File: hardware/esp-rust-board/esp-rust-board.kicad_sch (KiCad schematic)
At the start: 83 parts, among them J1 USB4105-GF-A, J2 MOTOR L, J3 MOTOR R, J4 BATT, J5 LED L, J6 LED R, Q1 DMG3415U, Q2 Si2319CDS, Q3 Si2319CDS, Q4 MMBT3904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

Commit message: Place components on PCB
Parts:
- removed J4: BATT, symbol Connector_Generic:Conn_01x02
- removed J5: LED L, Connector_JST:JST_PH_B2B-PH-SM4-TB_1x02-1MP_P2.00mm_Vertical, symbol Connector_Generic:Conn_01x02
- removed J6: LED R, Connector_JST:JST_PH_B2B-PH-SM4-TB_1x02-1MP_P2.00mm_Vertical, symbol Connector_Generic:Conn_01x02
- removed Q4, Q5: MMBT3904, Package_TO_SOT_SMD:SOT-23, symbol Transistor_BJT:MMBT3904
- removed R22, R24: 470R 1%, Resistor_SMD:R_0402_1005Metric, symbol Device:R_Small_US
- removed R23, R25: 10kR 1%, Resistor_SMD:R_0402_1005Metric, symbol Device:R_Small_US
- removed TP2: IMU_INT2, TestPoint:TestPoint_Pad_D1.0mm, symbol Connector:TestPoint
- added H1, H2: MountingHole_Pad, TestPoint:TestPoint_Keystone_5005-5009_Compact, symbol Mechanical:MountingHole_Pad
- added J7, J8: SERVO R, Connector_PinSocket_2.00mm:PinSocket_1x03_P2.00mm_Vertical, symbol Connector_Generic:Conn_01x03
- J2, J3: footprint Connector_JST:JST_PH_B2B-PH-SM4-TB_1x02-1MP_P2.00mm_Vertical -> Connector_PinHeader_2.00mm:PinHeader_1x02_P2.00mm_Vertical
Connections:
- net +BATT: now also H1.1, J7.2 (Pin_2), J8.2 (Pin_2)
- net GND: now also H2.1, J7.3 (Pin_3), J8.3 (Pin_3)
- net IO0: now also J7.1 (Pin_1)
- net IO20_RX: now also TP3.1; no longer TP1.1
- net IO21_TX: now also TP1.1; no longer TP3.1
- net IO4: now also R13.1
- net IO5: now also R20.1
- net IO6: now also J8.1 (Pin_1); no longer R20.1
- net IO7: now also R11.1; no longer R13.1
- net IO1: no longer names the net of U3.13 (GPIO1/ADC1_CH1/XTAL_32K_N)
- net IO2: no longer names the net of U3.5 (GPIO2/ADC1_CH2)
- net IO2: no longer R11.1
- net IO3: no longer names the net of U3.6 (GPIO3/ADC1_CH3)
- no-connect marks 18 -> 33
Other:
- note added: "Address: 0x0d (0001101b)"
- moved on the sheet: C12, C13, C17, C18, C20, C3, D11, J3, Q3, R12, R20, R21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

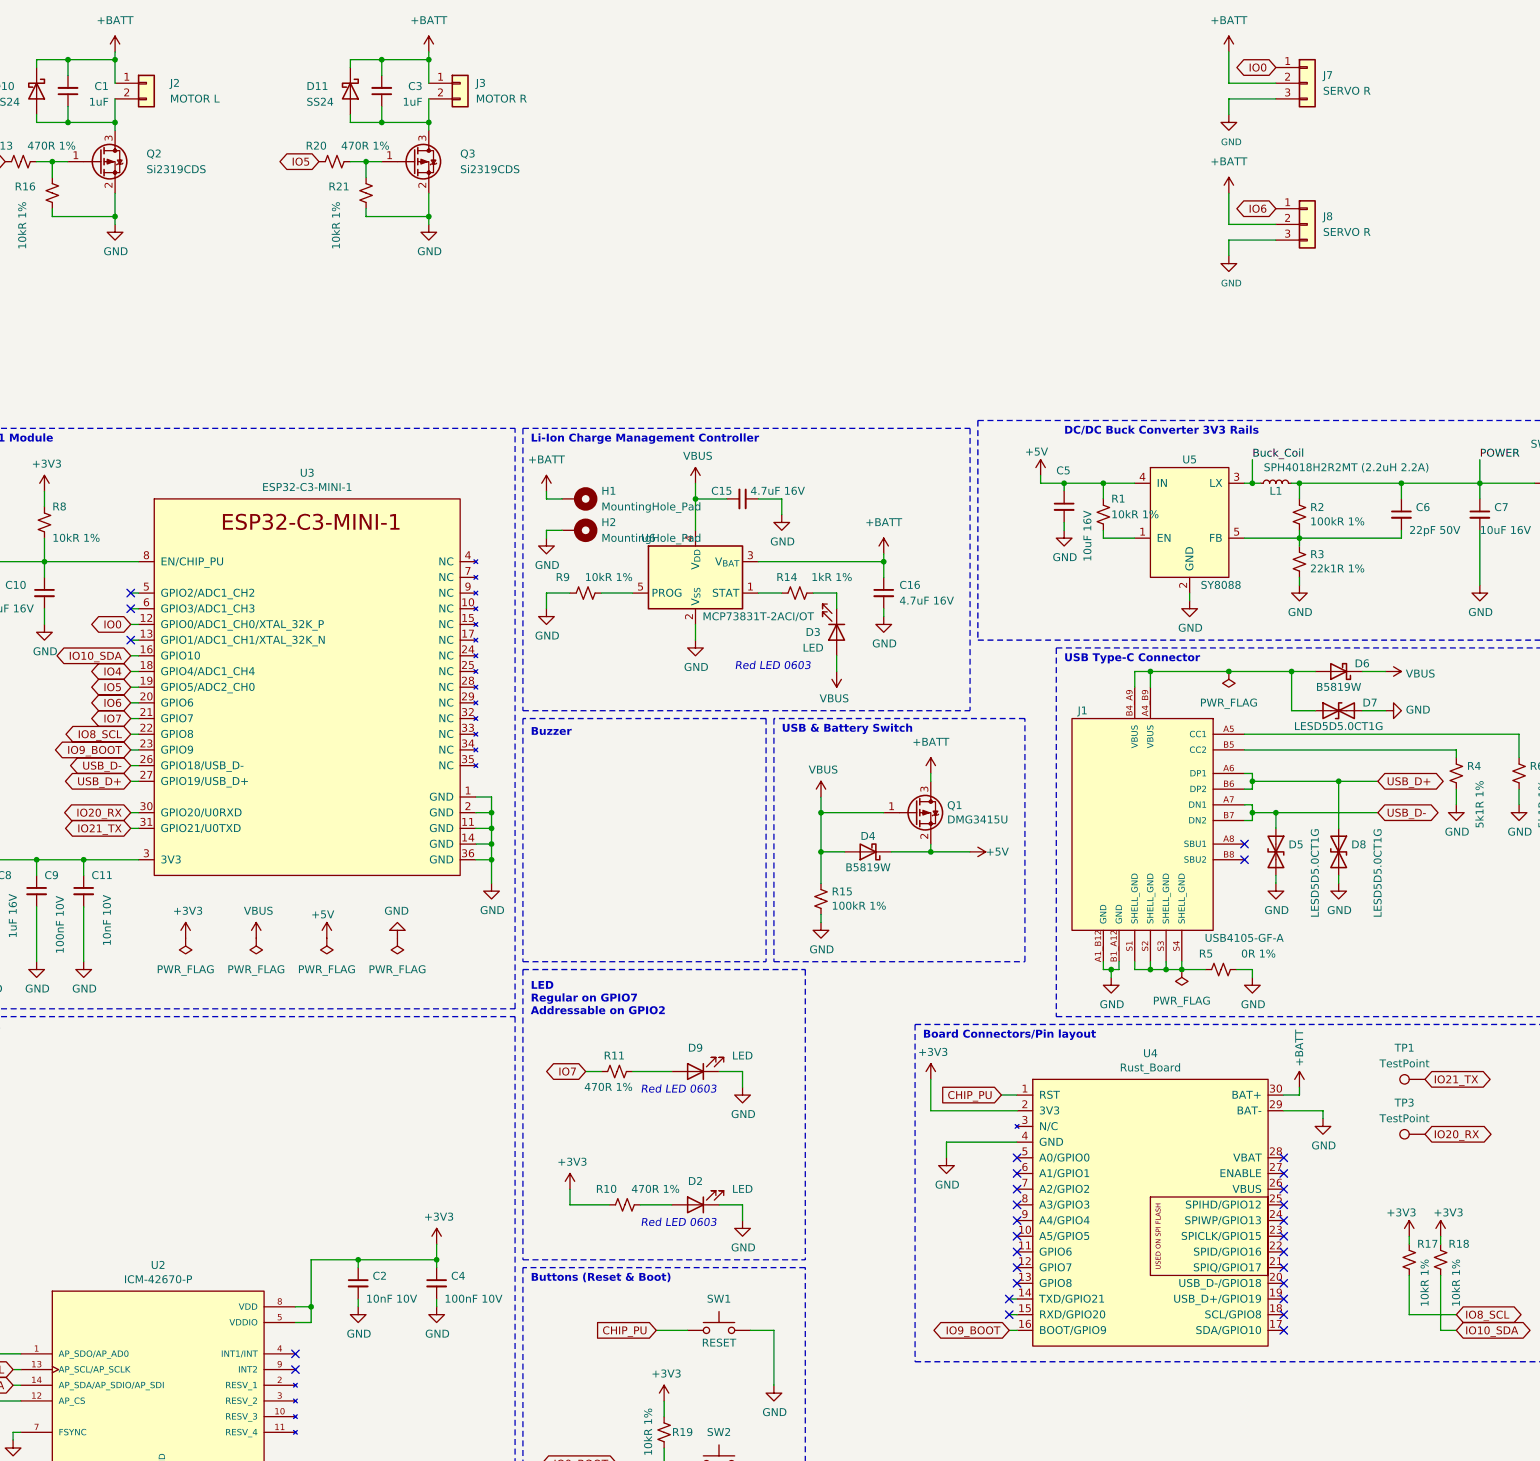
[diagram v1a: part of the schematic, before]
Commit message: Add missing LCSC parts
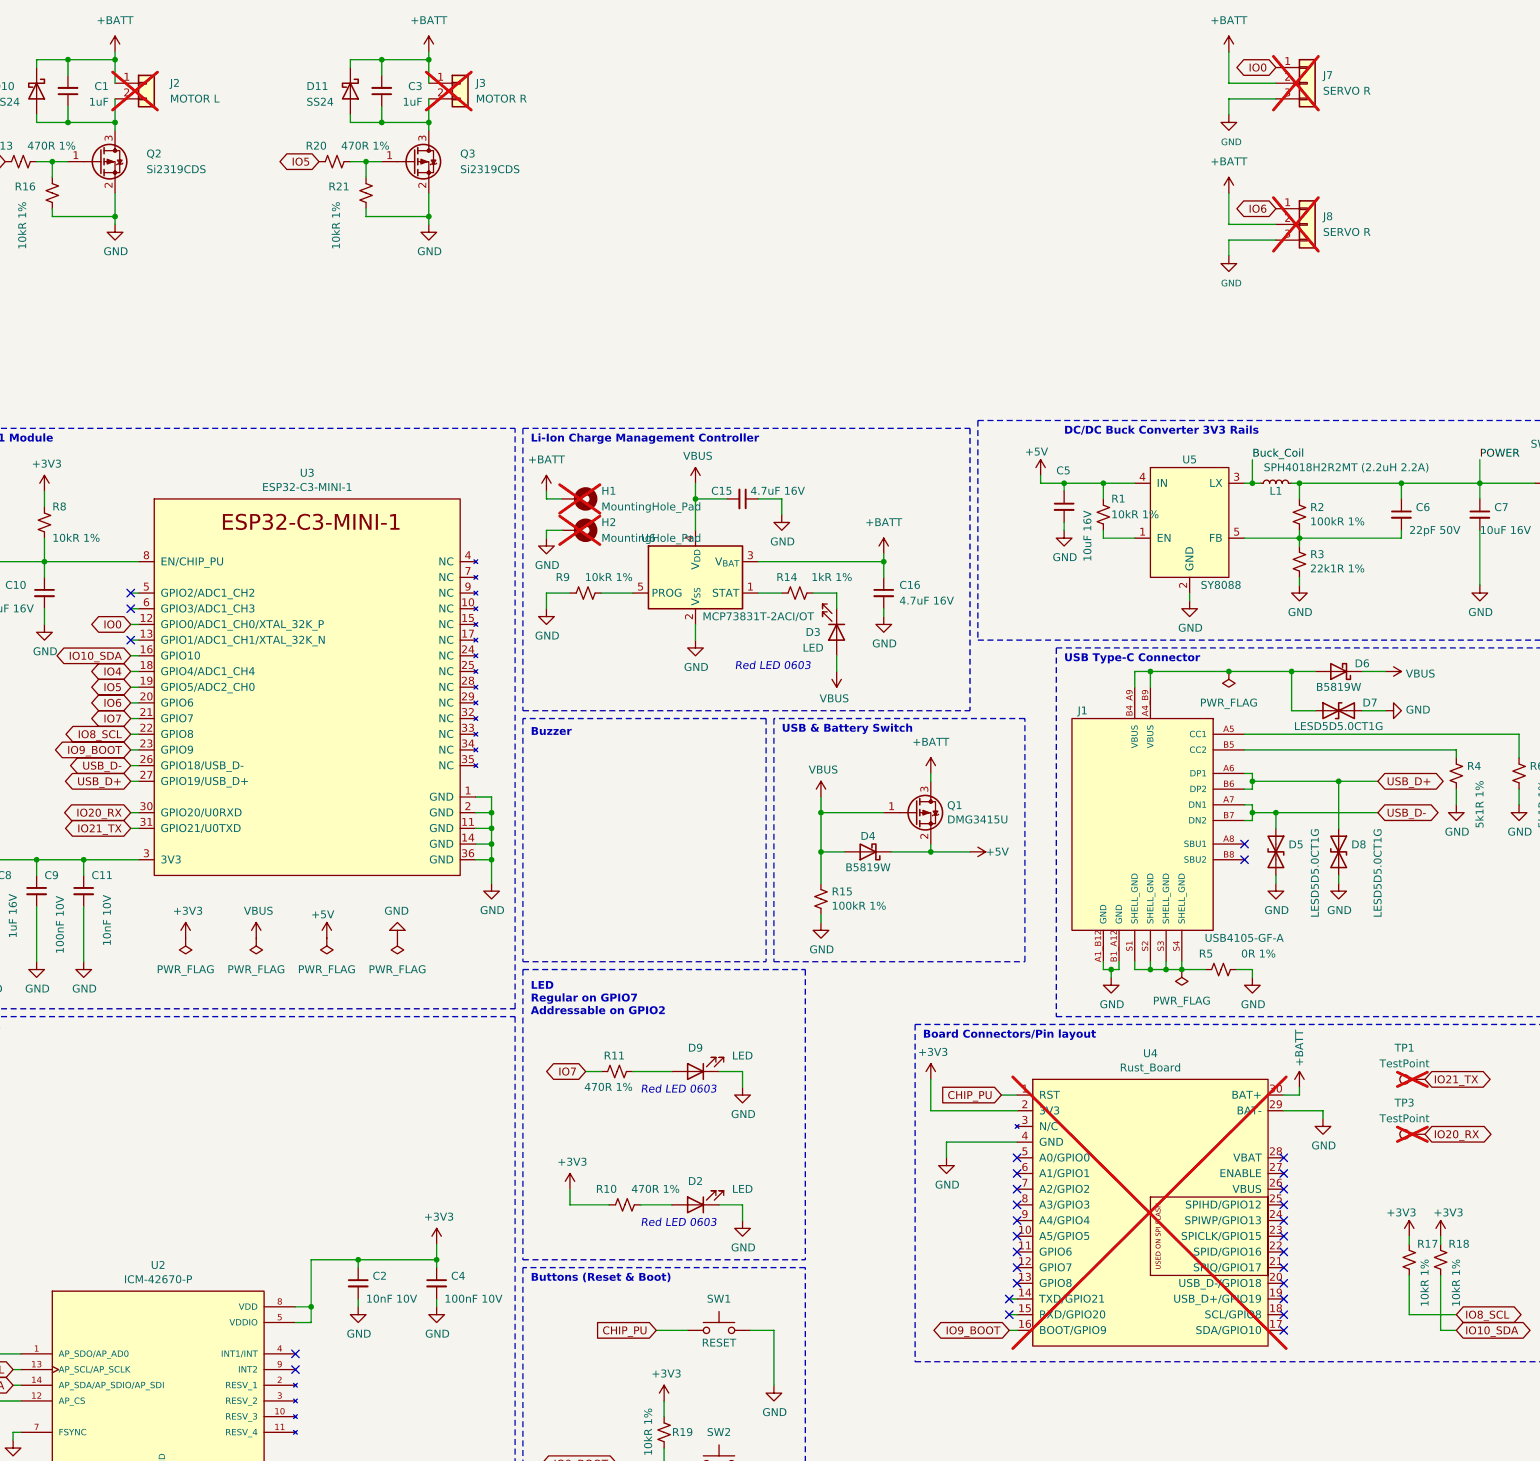
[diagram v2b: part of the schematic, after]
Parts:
- H1, H2, J2, J3, J7, J8, TP1, TP3, U4: now not fitted
- Q2, Q3: LCSC (none) -> C146287
- SW3: LCSC (none) -> C3008585
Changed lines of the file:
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@@
 		(in_bom no)
 		(on_board yes)
-		(dnp no)
+		(dnp yes)
 		(property "Reference" "U4"
 			(at 215.9 115.189 0)
@@
 		(in_bom yes)
 		(on_board yes)
-		(dnp no)
+		(dnp yes)
 		(fields_autoplaced yes)
 		(property "Reference" "J2"
@@
 		(in_bom yes)
 		(on_board yes)
-		(dnp no)
+		(dnp yes)
 		(fields_autoplaced yes)
 		(property "Reference" "J3"
@@
 			)
 		)
+		(property "LCSC" "C146287"
+			(at 45.72 -29.21 0)
+			(effects
+				(font
+					(size 1.27 1.27)
+				)
+				(hide yes)
+			)
+		)
 		(pin "3"
 		)
@@
 		(in_bom yes)
 		(on_board yes)
-		(dnp no)
+		(dnp yes)
 		(fields_autoplaced yes)
 		(property "Reference" "TP1"
@@
 		(in_bom yes)
 		(on_board yes)
-		(dnp no)
+		(dnp yes)
 		(fields_autoplaced yes)
 		(property "Reference" "TP3"
@@
 		(in_bom no)
 		(on_board yes)
-		(dnp no)
+		(dnp yes)
 		(fields_autoplaced yes)
 		(property "Reference" "H2"
@@
 			)
 		)
+		(property "LCSC" "C3008585"
+			(at 283.21 22.86 0)
+			(effects
+				(font
+					(size 1.27 1.27)
+				)
+				(hide yes)
+			)
+		)
 		(pin "2"
 		)
@@
 			)
 		)
+		(property "LCSC" "C146287"
+			(at 96.52 -29.21 0)
+			(effects
+				(font
+					(size 1.27 1.27)
+				)
+				(hide yes)
+			)
+		)
 		(pin "3"
 		)
@@
 		(in_bom no)
 		(on_board yes)
-		(dnp no)
+		(dnp yes)
 		(fields_autoplaced yes)
 		(property "Reference" "H1"
@@
 		(in_bom yes)
 		(on_board yes)
-		(dnp no)
+		(dnp yes)
 		(fields_autoplaced yes)
 		(property "Reference" "J8"
@@
 		(in_bom yes)
 		(on_board yes)
-		(dnp no)
+		(dnp yes)
 		(fields_autoplaced yes)
 		(property "Reference" "J7"

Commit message: Design completed
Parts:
- added J4: LED L, Connector_PinHeader_2.00mm:PinHeader_1x02_P2.00mm_Vertical, symbol Connector_Generic:Conn_01x02
- added Q4: MMBT3904, Package_TO_SOT_SMD:SOT-23, symbol Transistor_BJT:MMBT3904
- added R22: 470R 1%, Resistor_SMD:R_0402_1005Metric, symbol Device:R_Small_US
- added R23: 10kR 1%, Resistor_SMD:R_0402_1005Metric, symbol Device:R_Small_US
- C1, C3: value 1uF -> 1uF 16V
- C14, C21: now in the parts list
- D10, D11: LCSC C5380708 -> C5380709
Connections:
- net +BATT: now also J4.1 (Pin_1)
- net GND: now also Q4.2 (E), R23.2
- net IO0: now also R22.1; no longer J7.1 (Pin_1)
- net IO1: now reaches U3.13 (GPIO1/ADC1_CH1/XTAL_32K_N)
- net IO1: now also J7.1 (Pin_1)
- new net: Q4.1 (B), R22.2, R23.1
- new net: J4.2 (Pin_2), Q4.3 (C)
- no-connect marks 33 -> 32

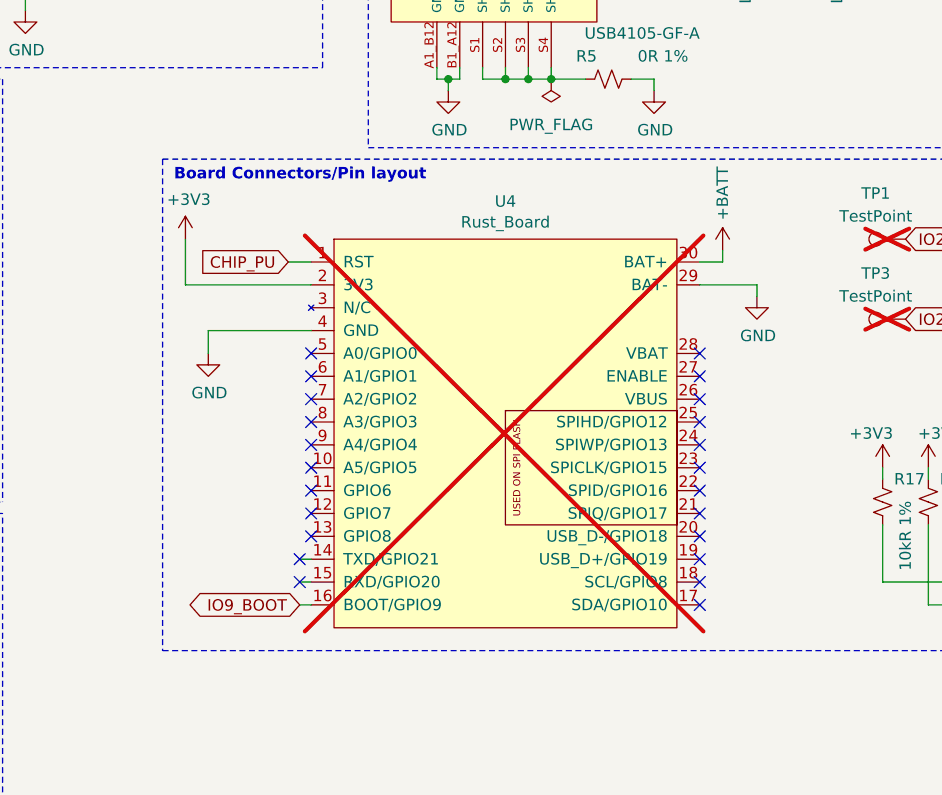
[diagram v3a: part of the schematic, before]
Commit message: Remove unused rust board
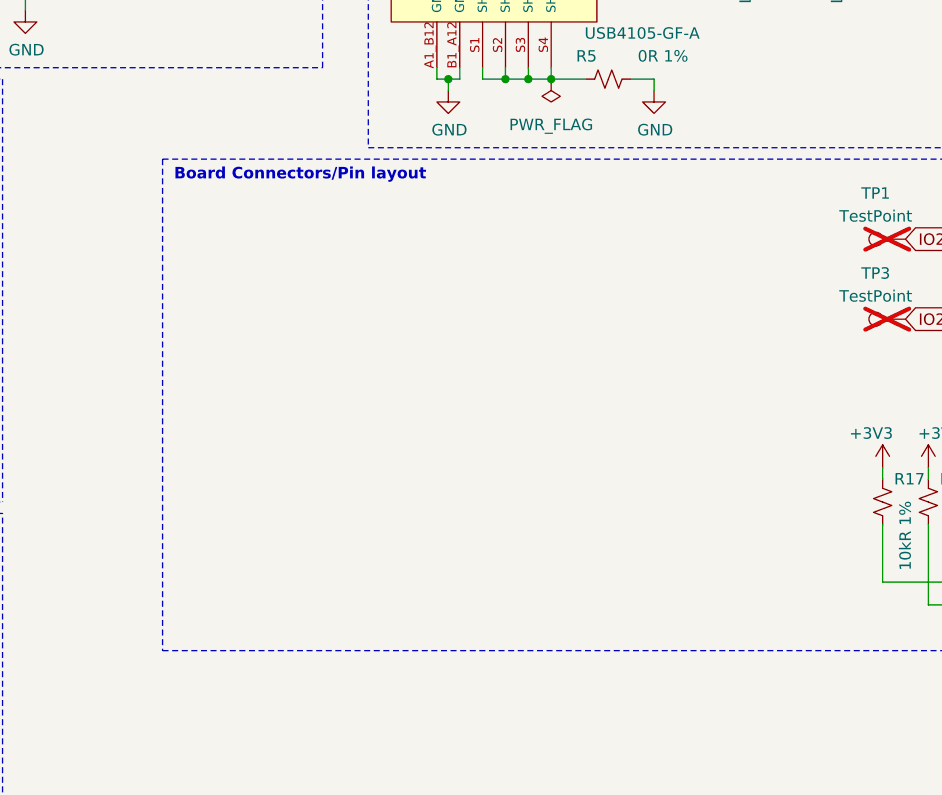
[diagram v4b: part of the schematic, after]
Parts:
- removed U4: Rust_Board, Rust_Board:Rust_Board, symbol Rust_Board:Rust_Board
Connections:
- no-connect marks 32 -> 9

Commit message: Update esp-rust-board.kicad_sch
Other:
- note added: "I2c Pull-up"
- note added: "Motor Drivers"
- note added: "Position LEDs"
- note added: "Servo Connectors"
- note removed: "Buzzer"
- moved on the sheet: C1, C12, C13, C17, C18, C19, C2, C20, C21, C3, C4, C5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
